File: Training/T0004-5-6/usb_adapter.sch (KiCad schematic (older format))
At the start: 23 parts, among them J1 modular8_rev3_comms_out, P1 USB_OTG, U1 FT231X, U2 TE_1825058-1

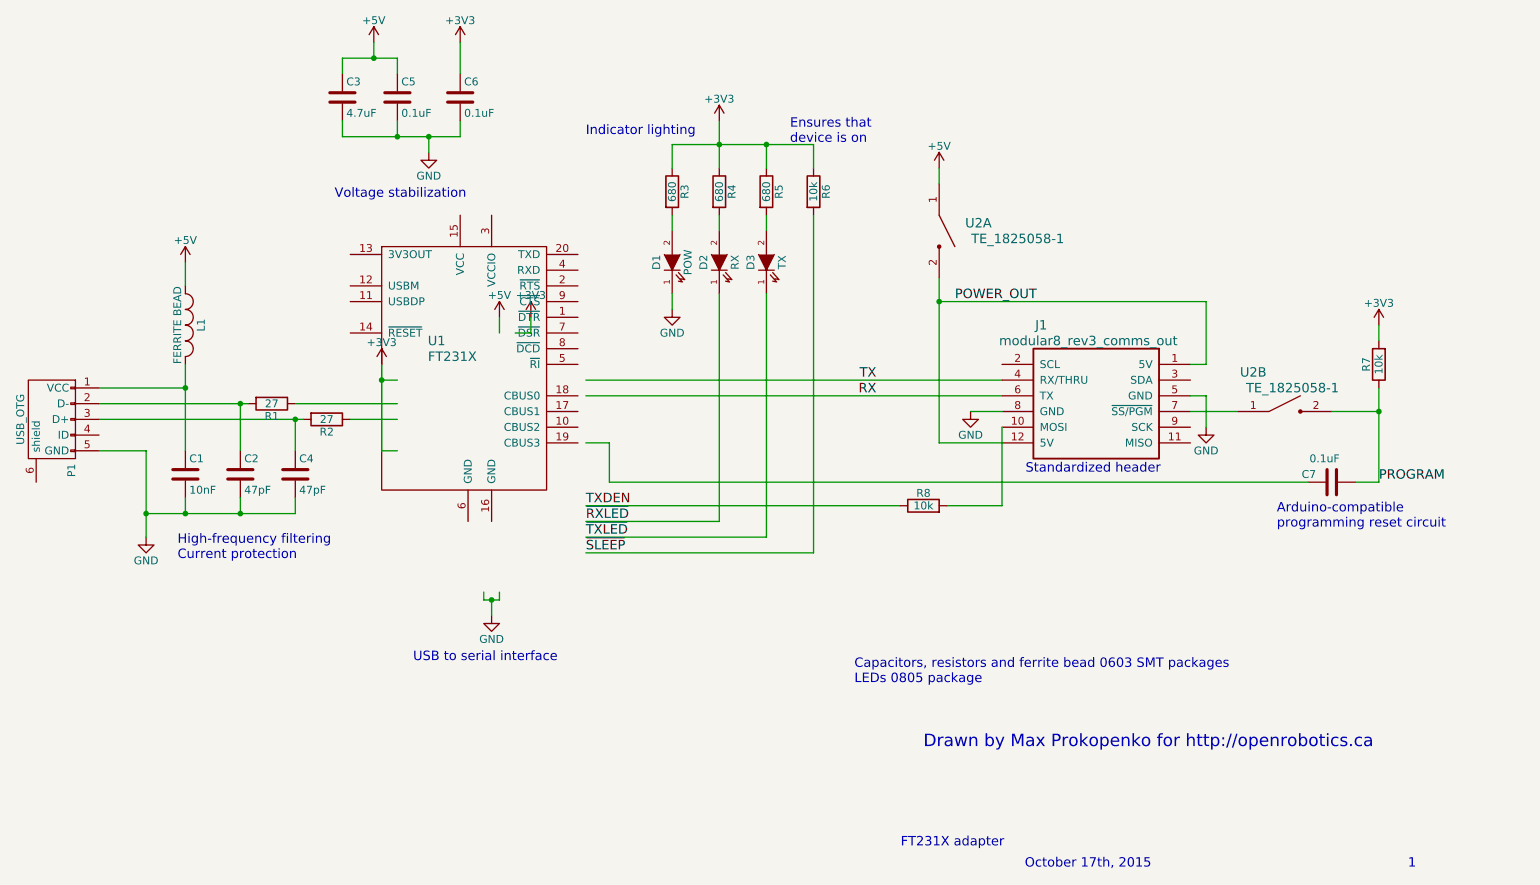
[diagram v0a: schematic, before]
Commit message: footprint fixes
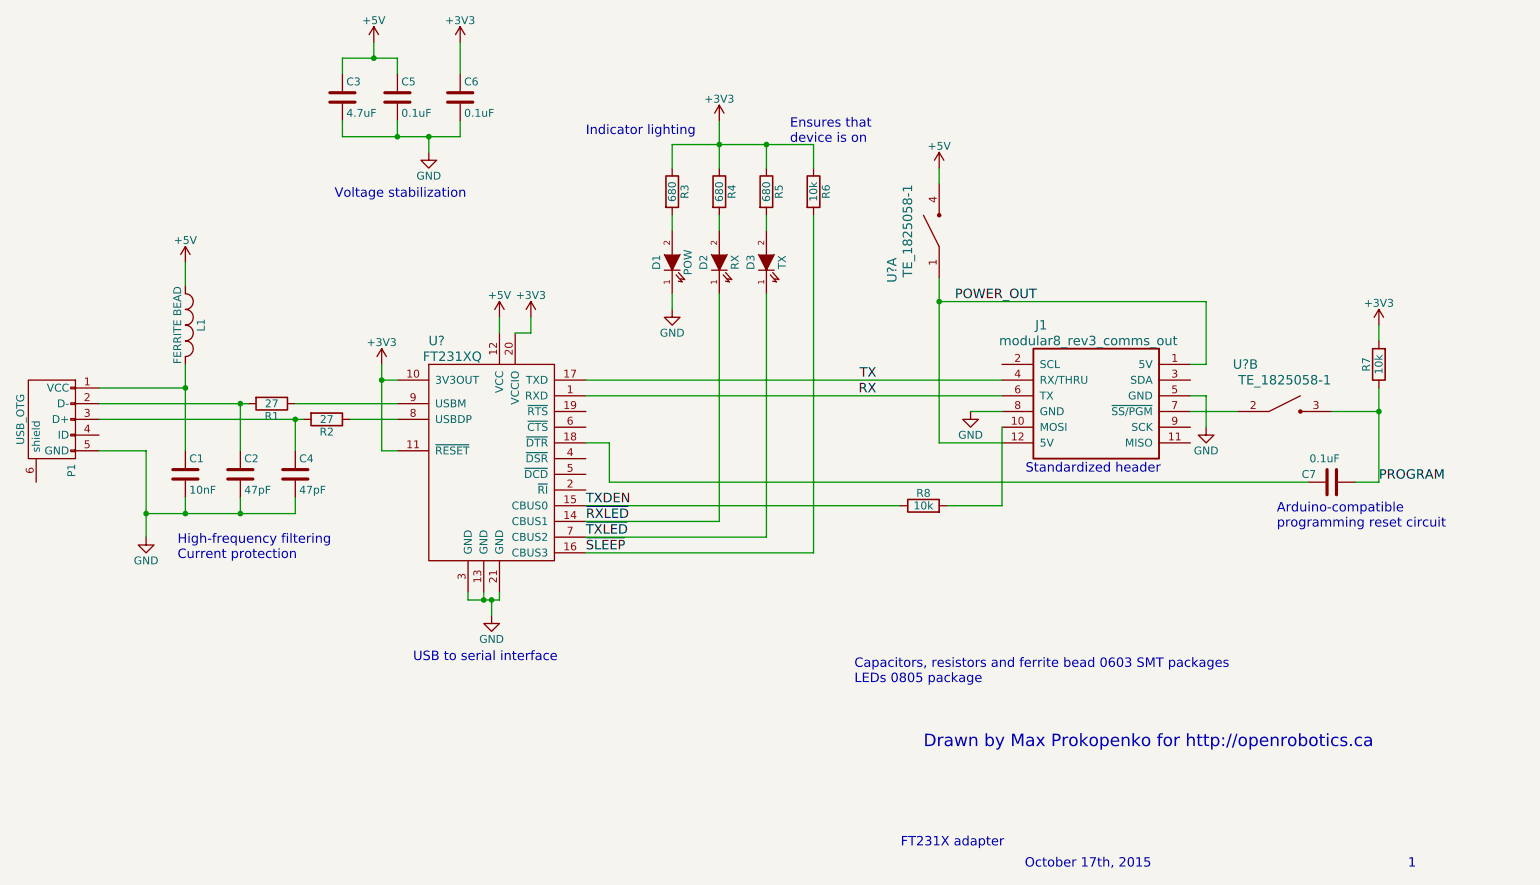
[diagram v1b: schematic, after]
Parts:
- removed U1: FT231X, Housings_DFN_QFN:QFN-20-1EP_4x4mm_Pitch0.5mm, symbol FT231X
- removed U2: TE_1825058-1, open_robotics:DIPSWITCH_SMT_ALCO_2CCT, symbol TE_1825058-1-RESCUE-usb_adapter
- added U?: FT231XQ, symbol FT231XQ
- added U? (x2): TE_1825058-1, symbol TE_1825058-1
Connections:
- wire segments 72 -> 73
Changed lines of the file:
@@
 1
-$Comp
-L FT231X U1
-U 1 1 5622A3C5
-P 4050 3600
-F 0 "U1" H 3700 4100 60  0000 C CNN
-F 1 "FT231X" H 3800 4000 60  0000 C CNN
-F 2 "Housings_DFN_QFN:QFN-20-1EP_4x4mm_Pitch0.5mm" H 4000 4100 60  0001 C CNN
-F 3 "" H 4000 4100 60  0000 C CNN
-	1    4050 3600
-	1    0    0    -1
-$EndComp
 $Comp
 L R R2
@@
 $EndComp
 $Comp
-L TE_1825058-1-RESCUE-usb_adapter U2
-U 1 1 5629AB3C
-P 6900 2400
-F 0 "U2" V 6850 2650 60  0000 C CNN
-F 1 "TE_1825058-1" V 6950 2900 60  0000 C CNN
-F 2 "open_robotics:DIPSWITCH_SMT_ALCO_2CCT" H 7010 2400 60  0001 C CNN
-F 3 "" H 7010 2400 60  0000 C CNN
-	1    6900 2400
-	0    1    1    0
-$EndComp
-$Comp
-L TE_1825058-1-RESCUE-usb_adapter U2
-U 2 1 5629ABC7
-P 9100 3550
-F 0 "U2" H 8900 3800 60  0000 C CNN
-F 1 "TE_1825058-1" H 9150 3700 60  0000 C CNN
-F 2 "open_robotics:DIPSWITCH_SMT_ALCO_2CCT" H 9210 3550 60  0001 C CNN
-F 3 "" H 9210 3550 60  0000 C CNN
-	2    9100 3550
-	1    0    0    -1
-$EndComp
-$Comp
 L modular8_rev3_comms_out J1
 U 1 1 5629AC49
@@
 	4000 4700 4000 4750
 Wire Wire Line
-	4000 4750 4100 4750
+	3900 4750 4100 4750
 Wire Wire Line
 	4100 4750 4100 4700
@@
 Text Notes 5950 1850 0    60   ~ 0
 Ensures that\ndevice is on
+$Comp
+L FT231XQ U?
+U 1 1 563E7BB9
+P 4050 3600
+F 0 "U?" H 3700 4100 60  0000 C CNN
+F 1 "FT231XQ" H 3800 4000 60  0000 C CNN
+F 2 "" H 4000 4100 60  0000 C CNN
+F 3 "" H 4000 4100 60  0000 C CNN
+	1    4050 3600
+	1    0    0    -1
+$EndComp
+Wire Wire Line
+	3900 4750 3900 4700
+Connection ~ 4000 4750
+$Comp
+L TE_1825058-1 U?
+U 1 1 563E7C92
+P 6900 2400
+F 0 "U?" H 6650 2700 60  0000 C CNN
+F 1 "TE_1825058-1" H 6900 2600 60  0000 C CNN
+F 2 "" H 7010 2400 60  0000 C CNN
+F 3 "" H 7010 2400 60  0000 C CNN
+	1    6900 2400
+	0    -1   -1   0
+$EndComp
+$Comp
+L TE_1825058-1 U?
+U 2 1 563E7D59
+P 9100 3550
+F 0 "U?" H 8850 3850 60  0000 C CNN
+F 1 "TE_1825058-1" H 9100 3750 60  0000 C CNN
+F 2 "" H 9210 3550 60  0000 C CNN
+F 3 "" H 9210 3550 60  0000 C CNN
+	2    9100 3550
+	1    0    0    -1
+$EndComp
 $EndSCHEMATC

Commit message: generated gerbers
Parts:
- U1: renamed from U?; footprint (none) -> Housings_DFN_QFN:QFN-20-1EP_4x4mm_Pitch0.5mm
- U2: renamed from U?; footprint (none) -> open_robotics:DIPSWITCH_SMT_ALCO_2CCT
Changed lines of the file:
@@
 Ensures that\ndevice is on
 $Comp
-L FT231XQ U?
+L FT231XQ U1
 U 1 1 563E7BB9
 P 4050 3600
-F 0 "U?" H 3700 4100 60  0000 C CNN
+F 0 "U1" H 3700 4100 60  0000 C CNN
 F 1 "FT231XQ" H 3800 4000 60  0000 C CNN
-F 2 "" H 4000 4100 60  0000 C CNN
+F 2 "Housings_DFN_QFN:QFN-20-1EP_4x4mm_Pitch0.5mm" H 4000 4100 60  0001 C CNN
 F 3 "" H 4000 4100 60  0000 C CNN
 	1    4050 3600
@@
 Connection ~ 4000 4750
 $Comp
-L TE_1825058-1 U?
+L TE_1825058-1 U2
 U 1 1 563E7C92
 P 6900 2400
-F 0 "U?" H 6650 2700 60  0000 C CNN
+F 0 "U2" H 6650 2700 60  0000 C CNN
 F 1 "TE_1825058-1" H 6900 2600 60  0000 C CNN
-F 2 "" H 7010 2400 60  0000 C CNN
+F 2 "open_robotics:DIPSWITCH_SMT_ALCO_2CCT" H 7010 2400 60  0001 C CNN
 F 3 "" H 7010 2400 60  0000 C CNN
 	1    6900 2400
@@
 $EndComp
 $Comp
-L TE_1825058-1 U?
+L TE_1825058-1 U2
 U 2 1 563E7D59
 P 9100 3550
-F 0 "U?" H 8850 3850 60  0000 C CNN
+F 0 "U2" H 8850 3850 60  0000 C CNN
 F 1 "TE_1825058-1" H 9100 3750 60  0000 C CNN
-F 2 "" H 9210 3550 60  0000 C CNN
+F 2 "open_robotics:DIPSWITCH_SMT_ALCO_2CCT" H 9210 3550 60  0001 C CNN
 F 3 "" H 9210 3550 60  0000 C CNN
 	2    9100 3550
